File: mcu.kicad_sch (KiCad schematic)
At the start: 0 parts

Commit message: Created symbol/footprint for MCU & rotary encoder
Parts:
- added SW1: SW_Rotary_1x8_MP, symbol Switch:SW_Rotary_1x8_MP
- added U2: ESP32-DEVKITC-32UE, ESP32-DEVKITC-32UE:ESPRESSIF_ESP32-DEVKITC-32UE, symbol ESP32-DEVKITC-32UE:ESP32-DEVKITC-32UE
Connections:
- new net 3V3: SW1.9, U2.1 (3V3)
- new net 5V: U2.19 (5V)
- new net Earth: U2.14 (GND), U2.20 (GND__1), U2.26 (GND__2)
- new net RotaryOut: U2.11 (27)
- no-connect marks 0 -> 1

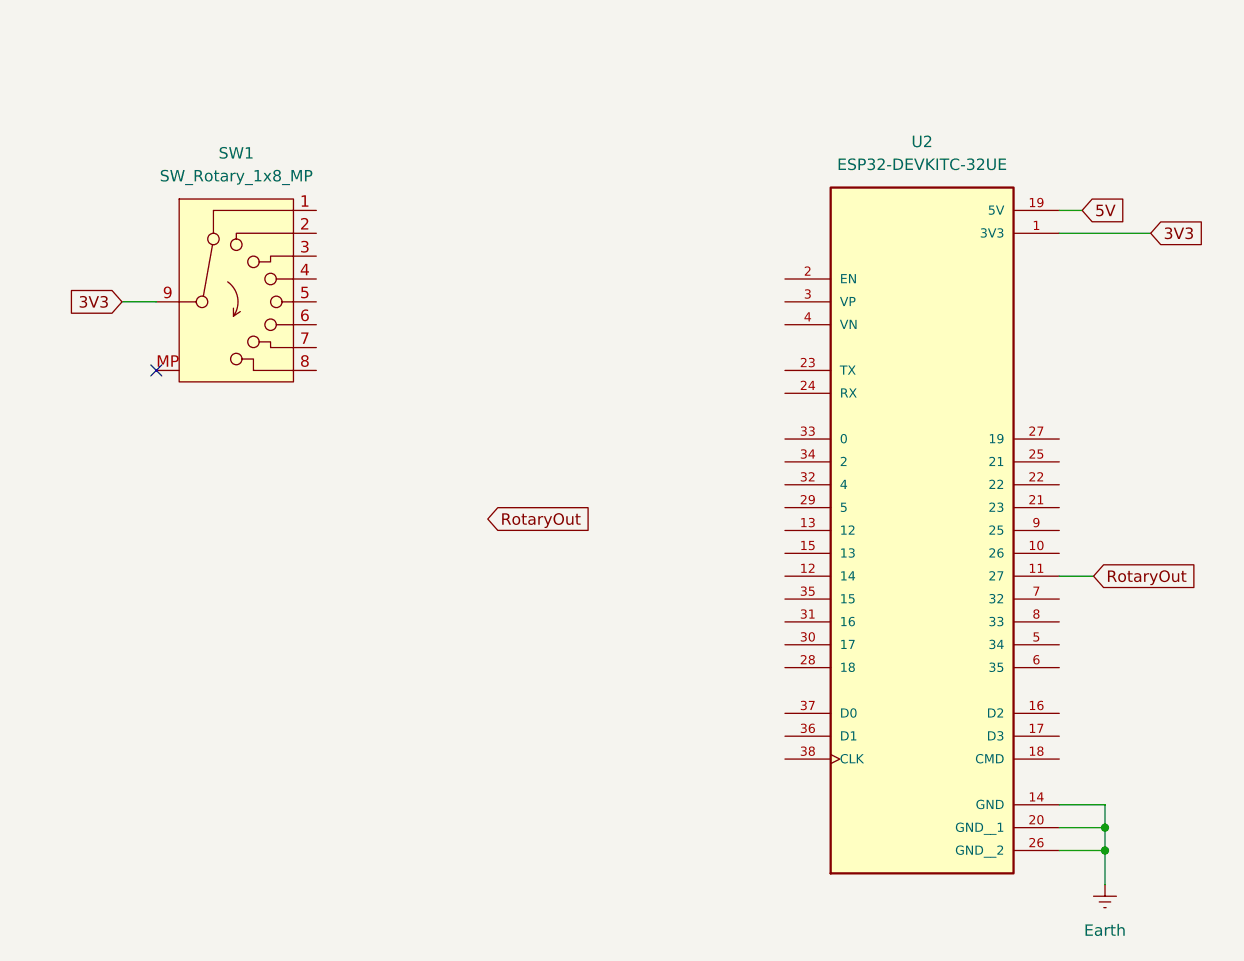
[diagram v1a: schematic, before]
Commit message: Finished rotary switch and updated MCU pinout
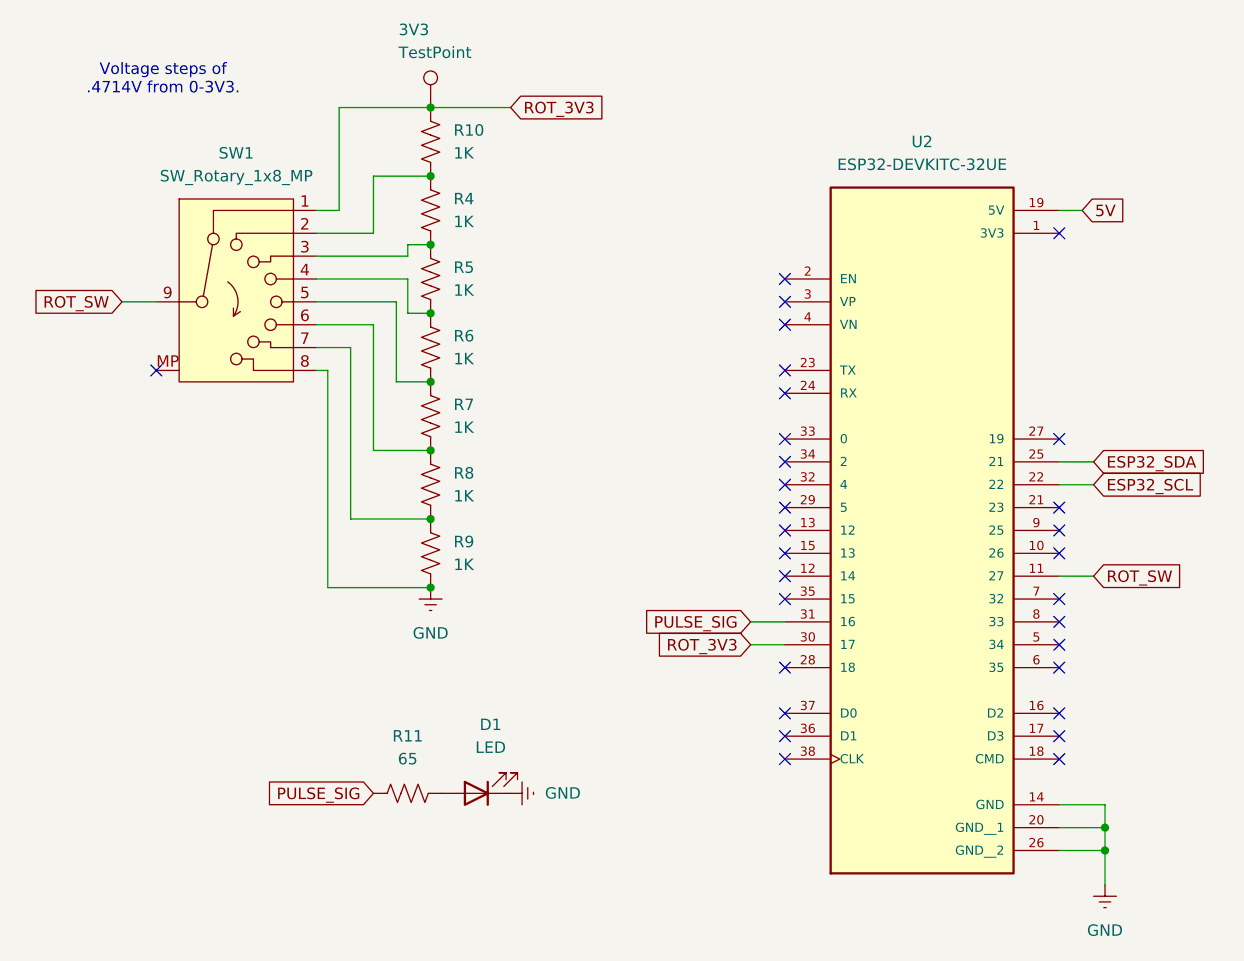
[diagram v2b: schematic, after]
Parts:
- added 3V3: TestPoint, symbol Connector:TestPoint
- added D1: LED, LED_SMD:LED_0805_2012Metric_Pad1.15x1.40mm_HandSolder, symbol Device:LED
- added R10, R4, R5, R6, R7, R8, R9: 1K, Resistor_SMD:R_0805_2012Metric_Pad1.20x1.40mm_HandSolder, symbol Device:R_US
- added R11: 65, Resistor_SMD:R_0805_2012Metric_Pad1.20x1.40mm_HandSolder, symbol Device:R_US
- SW1: footprint (none) -> ROT_SW2925:2925_ADA
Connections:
- net Earth is gone; now on net GND: U2.14 (GND), U2.20 (GND__1), U2.26 (GND__2)
- net ROT_3V3: now reaches SW1.1
- net ROT_3V3: now also U2.30 (17), 3V3.1, R10.1
- net at SW1.2: now also R10.2, R4.1
- net at SW1.3: now also R4.2, R5.1
- net at SW1.4: now also R5.2, R6.1
- net at SW1.5: now also R6.2, R7.1
- net at SW1.6: now also R7.2, R8.1
- net at SW1.7: now also R8.2, R9.1
- net GND: now reaches SW1.8
- net GND: now also D1.1 (K), R9.2
- net ESP32_SCL: now reaches U2.22
- net ESP32_SDA: now reaches U2.25 (21)
- net PULSE_SIG: now reaches U2.31 (16)
- net PULSE_SIG: now also R11.1
- net 3V3: no longer names the net of U2.1 (3V3)
- net 3V3: no longer SW1.9
- net RotaryOut renamed ROT_SW
- net ROT_SW: now also SW1.9
- new net: D1.2 (A), R11.2
- no-connect marks 1 -> 30
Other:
- note added: "Voltage steps of .4714V from 0-3V3."

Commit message: Updated references after merging
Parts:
- renumbered D1 to D2, R10 to R12, R4 to R13, R5 to R14, R6 to R15, R7 to R16, R8 to R17, R9 to R18, U2 to U3
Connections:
- net PULSE_SIG: no longer U3.31 (16)
- net DRV_A: now reaches U3.7 (32)
- net DRV_B: now reaches U3.8 (33)
- net 5V renamed +5V
- no-connect marks 30 -> 29

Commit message: Updated footprints of passive elements to be 0805 Hand-Solder
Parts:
- 3V3: footprint (none) -> TestPoint:TestPoint_Keystone_5019_Minature
- U3: footprint ESP32-DEVKITC-32UE:ESPRESSIF_ESP32-DEVKITC-32UE -> ESP32-DEVKITC_32UE:ESPRESSIF_ESP32-DEVKITC-32UE
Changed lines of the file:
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@@
 			)
 		)
-		(property "Footprint" "ESP32-DEVKITC-32UE:ESPRESSIF_ESP32-DEVKITC-32UE"
+		(property "Footprint" "ESP32-DEVKITC_32UE:ESPRESSIF_ESP32-DEVKITC-32UE"
 			(at 135.89 81.28 0)
 			(effects
@@
 			)
 		)
-		(property "Footprint" ""
+		(property "Footprint" "TestPoint:TestPoint_Keystone_5019_Minature"
 			(at 86.36 36.83 0)
 			(effects
